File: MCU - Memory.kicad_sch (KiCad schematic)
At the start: 10 parts, among them IC1 W9864G6KH-6

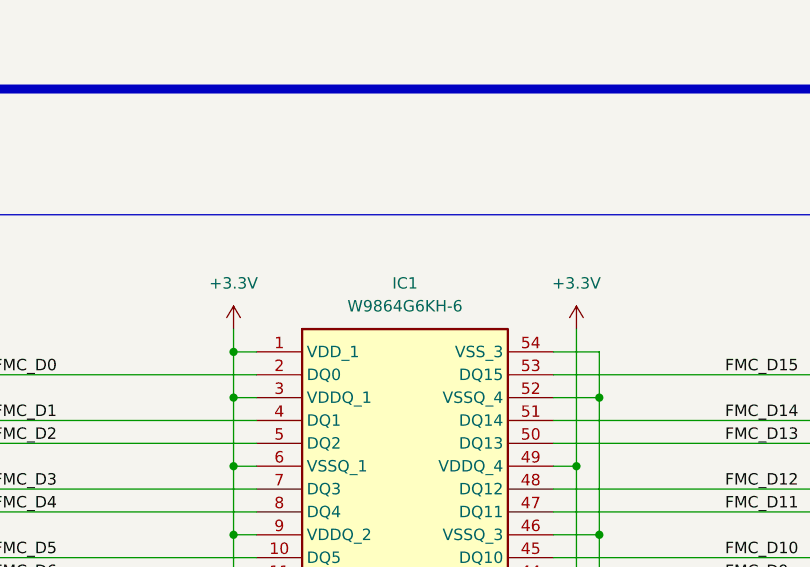
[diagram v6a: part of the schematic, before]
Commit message: designator chagnes and cleanup silkscreen
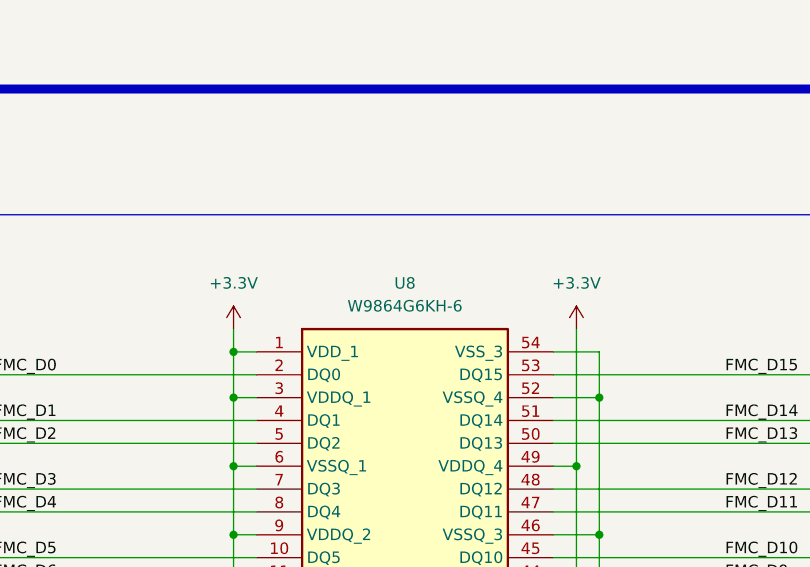
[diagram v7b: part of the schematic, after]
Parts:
- C1, C2, C3, C4, C5, C6, C7, C86, C87: LCSC PN (none) -> C1525
- U8: renamed from IC1; LCSC PN (none) -> C62378
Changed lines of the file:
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@@
+		(polyline
+			(pts
+				(xy 173.99 182.88) (xy 179.07 182.88) (xy 179.07 119.38) (xy 173.99 119.38)
+			)
+			(stroke
+				(width 0)
+				(type dash)
+			)
+			(fill
+				(type none)
+			)
+		)
+	)
+	(rule_area
 		(polyline
 			(pts
 				(xy 231.14 182.88) (xy 236.22 182.88) (xy 236.22 119.38) (xy 231.14 119.38)
-			)
-			(stroke
-				(width 0)
-				(type dash)
-			)
-			(fill
-				(type none)
-			)
-		)
-	)
-	(rule_area
-		(polyline
-			(pts
-				(xy 173.99 182.88) (xy 179.07 182.88) (xy 179.07 119.38) (xy 173.99 119.38)
 			)
 			(stroke
@@
 		)
 		(property "Supplier Part Number 1" "C1525"
+			(at 129.54 55.88 0)
+			(effects
+				(font
+					(size 1.27 1.27)
+				)
+				(hide yes)
+			)
+		)
+		(property "LCSC PN" "C1525"
 			(at 129.54 55.88 0)
 			(effects
@@
 			)
 		)
+		(property "LCSC PN" "C1525"
+			(at 198.12 55.88 0)
+			(effects
+				(font
+					(size 1.27 1.27)
+				)
+				(hide yes)
+			)
+		)
 		(pin "1"
 		)
@@
 			)
 		)
+		(property "LCSC PN" "C1525"
+			(at 219.71 55.88 0)
+			(effects
+				(font
+					(size 1.27 1.27)
+				)
+				(hide yes)
+			)
+		)
 		(pin "1"
 		)
@@
 		)
 		(property "Supplier Part Number 1" "C1525"
+			(at 152.4 55.88 0)
+			(effects
+				(font
+					(size 1.27 1.27)
+				)
+				(hide yes)
+			)
+		)
+		(property "LCSC PN" "C1525"
 			(at 152.4 55.88 0)
 			(effects
@@
 			)
 		)
+		(property "LCSC PN" "C1525"
+			(at 140.97 55.88 0)
+			(effects
+				(font
+					(size 1.27 1.27)
+				)
+				(hide yes)
+			)
+		)
 		(pin "1"
 		)
@@
 		(dnp no)
 		(fields_autoplaced yes)
-		(property "Reference" "IC1"
+		(property "Reference" "U8"
 			(at 204.47 110.49 0)
 			(effects
@@
 		)
 		(property "Supplier Part Number 1" "C62378"
+			(at 187.96 118.11 0)
+			(effects
+				(font
+					(size 1.27 1.27)
+				)
+				(hide yes)
+			)
+		)
+		(property "LCSC PN" "C62378"
 			(at 187.96 118.11 0)
 			(effects
@@
 			(project ""
 				(path "/0650c7a8-acba-429c-9f8e-eec0baf0bc1c/fede4c36-00cc-4d3d-b71c-5243ba232202/5817bdb2-adca-4121-9c7c-32ec97928e05"
-					(reference "IC1")
+					(reference "U8")
 					(unit 1)
 				)
@@
 			)
 		)
+		(property "LCSC PN" "C1525"
+			(at 163.83 55.88 0)
+			(effects
+				(font
+					(size 1.27 1.27)
+				)
+				(hide yes)
+			)
+		)
 		(pin "1"
 		)
@@
 		)
 		(property "Supplier Part Number 1" "C1525"
+			(at 186.69 55.88 0)
+			(effects
+				(font
+					(size 1.27 1.27)
+				)
+				(hide yes)
+			)
+		)
+		(property "LCSC PN" "C1525"
 			(at 186.69 55.88 0)
 			(effects
@@
 			)
 		)
+		(property "LCSC PN" "C1525"
+			(at 175.26 55.88 0)
+			(effects
+				(font
+					(size 1.27 1.27)
+				)
+				(hide yes)
+			)
+		)
 		(pin "1"
 		)
@@
 			(at 208.28 55.88 0)
 			(effects
+				(font
+					(size 1.27 1.27)
+				)
+				(hide yes)
+			)
+		)
+		(property "LCSC PN" "C1525"
+			(at 208.28 55.88 0)
+			(effects
